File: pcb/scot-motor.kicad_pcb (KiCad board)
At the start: 2 copper layers, 115.1 x 80.1 mm, 84 parts, among them IC1 MCP2562, IC2 STM32F0xxKxTx, IC3 NCV8450A, J1 Conn_01x03_Female, J2 Conn_01x03_Female, J3 Conn_01x02_Female, J4 Conn_01x03_Female, J5 Conn_01x02_Female, J6 Conn_01x02_Female, J7 Conn_01x02_Female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

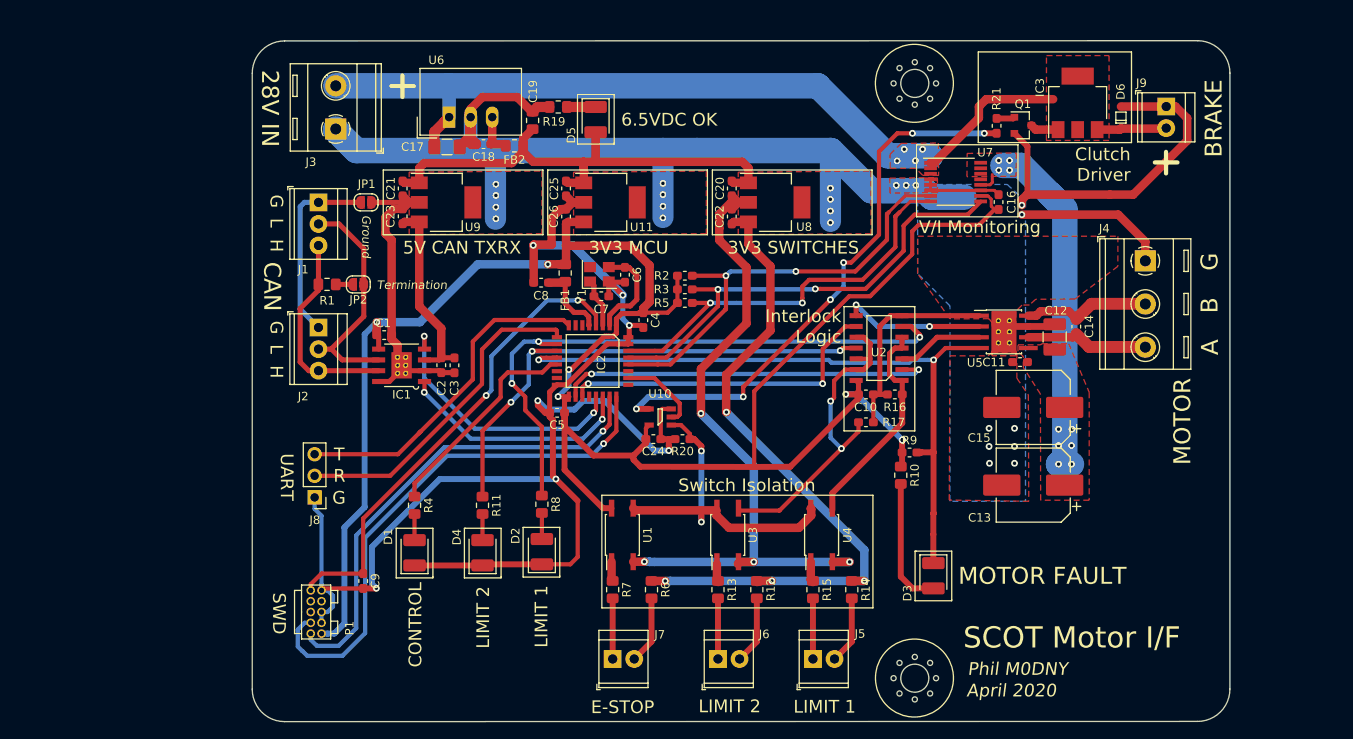
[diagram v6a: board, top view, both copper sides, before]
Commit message: pcb: Add Clutch Release indicator.
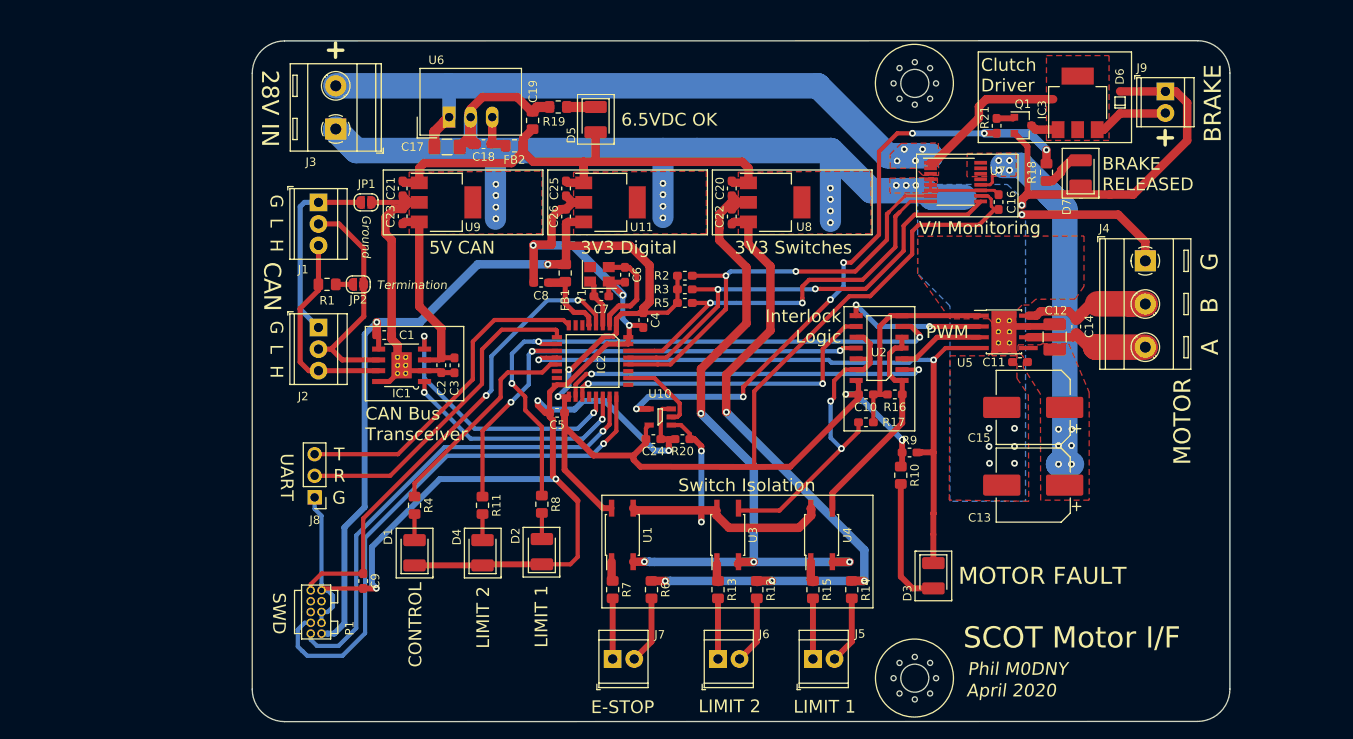
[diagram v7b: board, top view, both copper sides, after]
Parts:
- added D7: LED, LED_SMD:LED_1210_3225Metric_Pad1.42x2.65mm_HandSolder, F.Cu at (162.5, 58.5)
- added R18: 18R, Resistor_SMD:R_0805_2012Metric_Pad1.15x1.40mm_HandSolder, F.Cu at (158.5, 58.5)
- moved D6 1.78 mm to (167.2, 50.2)
- moved J9 1.78 mm to (172.5, 48.9)
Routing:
- net Net-(R18-Pad1): track 65.4 -> 75.1 mm, vias 6 -> 7
- net /MCU/MOTOR_A: track 14.6 -> 20.4 mm
- net /MCU/MOTOR_B: track 15.1 -> 20.7 mm
- net Net-(D7-Pad2): track 0.00 -> 5.17 mm
- net GND: track 535.9 -> 538.8 mm
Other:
- board text added: "3V3 Digital"
- board text added: "3V3 Switches"
- board text added: "5V CAN"
- board text added: "BRAKE RELEASED"
- board text added: "CAN Bus Transceiver"
- board text added: "PWM"
- board text removed: "3V3 MCU"
- board text removed: "3V3 SWITCHES"
- board text removed: "5V CAN TXRX"

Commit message: pcb: Final tweaks.
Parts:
- C18: value 1u/6.5V -> 4u7/6.5V; footprint Capacitor_SMD:C_0603_1608Metric_Pad1.05x0.95mm_HandSolder -> Capacitor_SMD:C_0805_2012Metric_Pad1.15x1.40mm_HandSolder
- moved FB2 0.80 mm to (96.7, 55.3)
- moved C18 0.40 mm to (92.6, 55.3)
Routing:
- net GND: track 538.8 -> 540.1 mm
- net /Power Supplies/6V5_SWREG: track 59.0 -> 59.9 mm
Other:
- board text added: "Shield to Gnd"
- board text removed: "Ground"
